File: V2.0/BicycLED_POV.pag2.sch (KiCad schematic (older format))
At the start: 136 parts, among them U10 74x595, U11 74x595, U12 74x595, U13 74x595, U14 74x595, U7 74x595, U8 74x595, U9 74x595

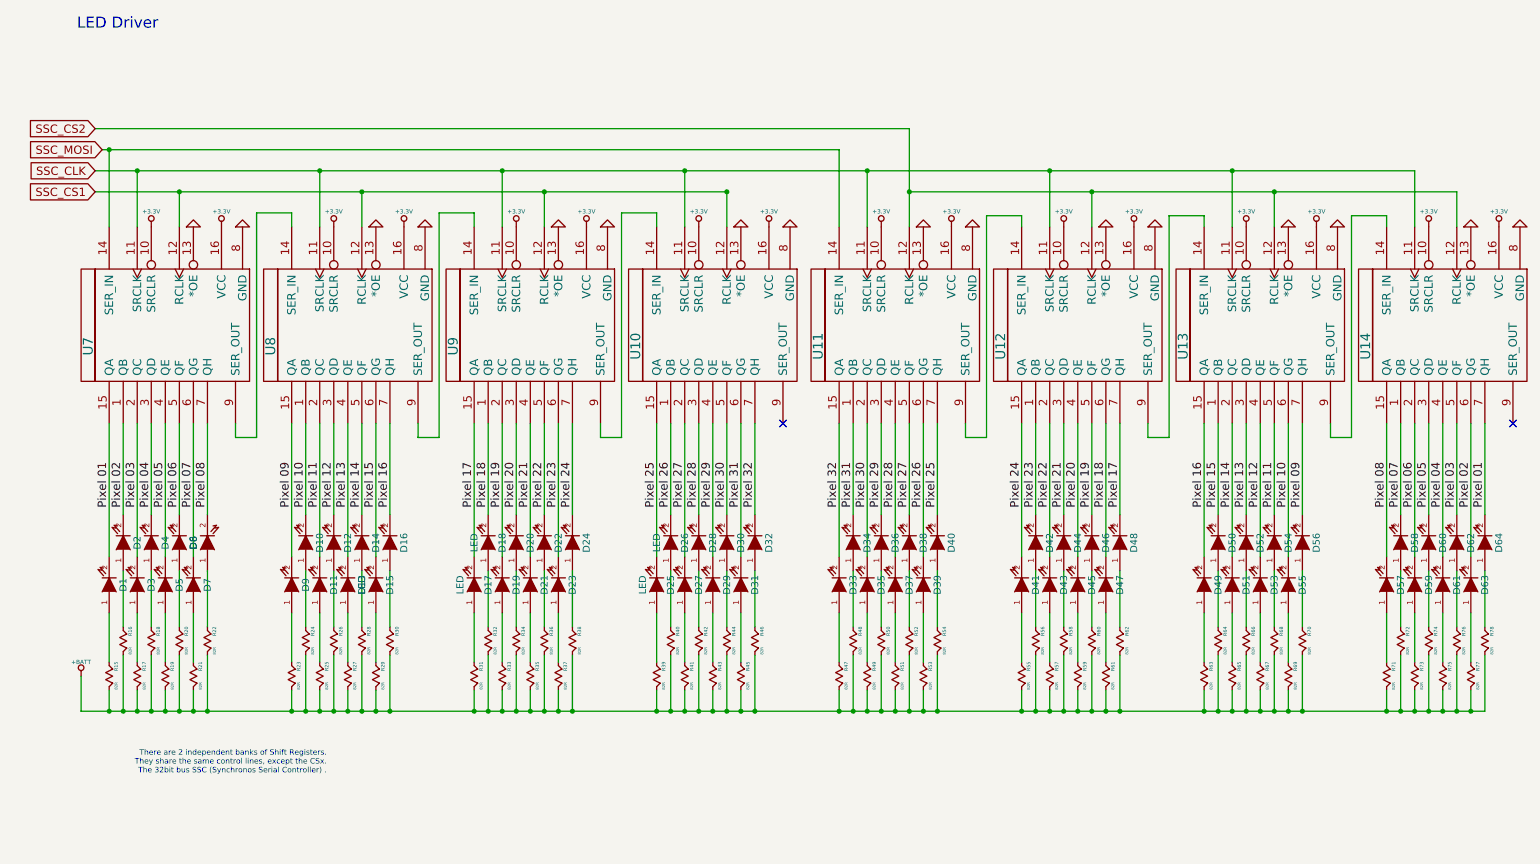
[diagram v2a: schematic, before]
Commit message: Symbols and Modules modifications.
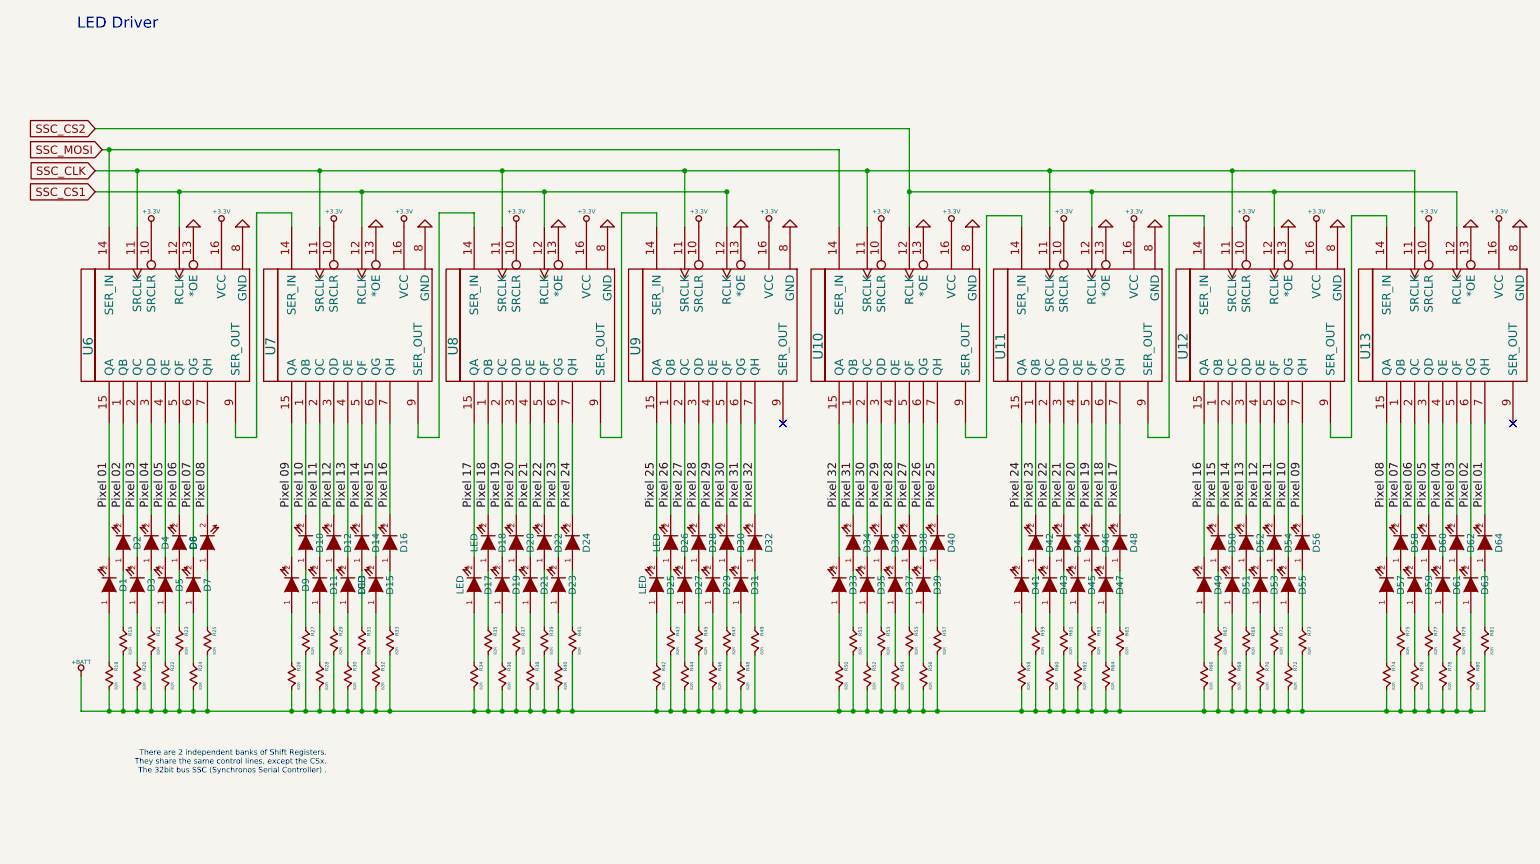
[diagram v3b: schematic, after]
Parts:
- renumbered R15 to R18, R16 to R19, R17 to R20, R18 to R21, R19 to R22, R20 to R23, R21 to R24, R22 to R25, R23 to R26, R24 to R27, R25 to R28, R26 to R29, R27 to R30, R28 to R31, R29 to R32, R30 to R33, R31 to R34, R32 to R35, R33 to R36, R34 to R37, R35 to R38, R36 to R39, R37 to R40, R38 to R41, R39 to R42, R40 to R43, R41 to R44, R42 to R45, R43 to R46, R44 to R47, R45 to R48, R46 to R49, R47 to R50, R48 to R51, R49 to R52, R50 to R53, R51 to R54, R52 to R55, R53 to R56, R54 to R57, R55 to R58, R56 to R59, R57 to R60, R58 to R61, R59 to R62, R60 to R63, R61 to R64, R62 to R65, R63 to R66, R64 to R67, R65 to R68, R66 to R69, R67 to R70, R68 to R71, R69 to R72, R70 to R73, R71 to R74, R72 to R75, R73 to R76, R74 to R77, R75 to R78, R76 to R79, R77 to R80, R78 to R81, U11 to U10, U12 to U11, U13 to U12, U14 to U13, U7 to U6, U8 to U7, U9 to U8, U10 to U9

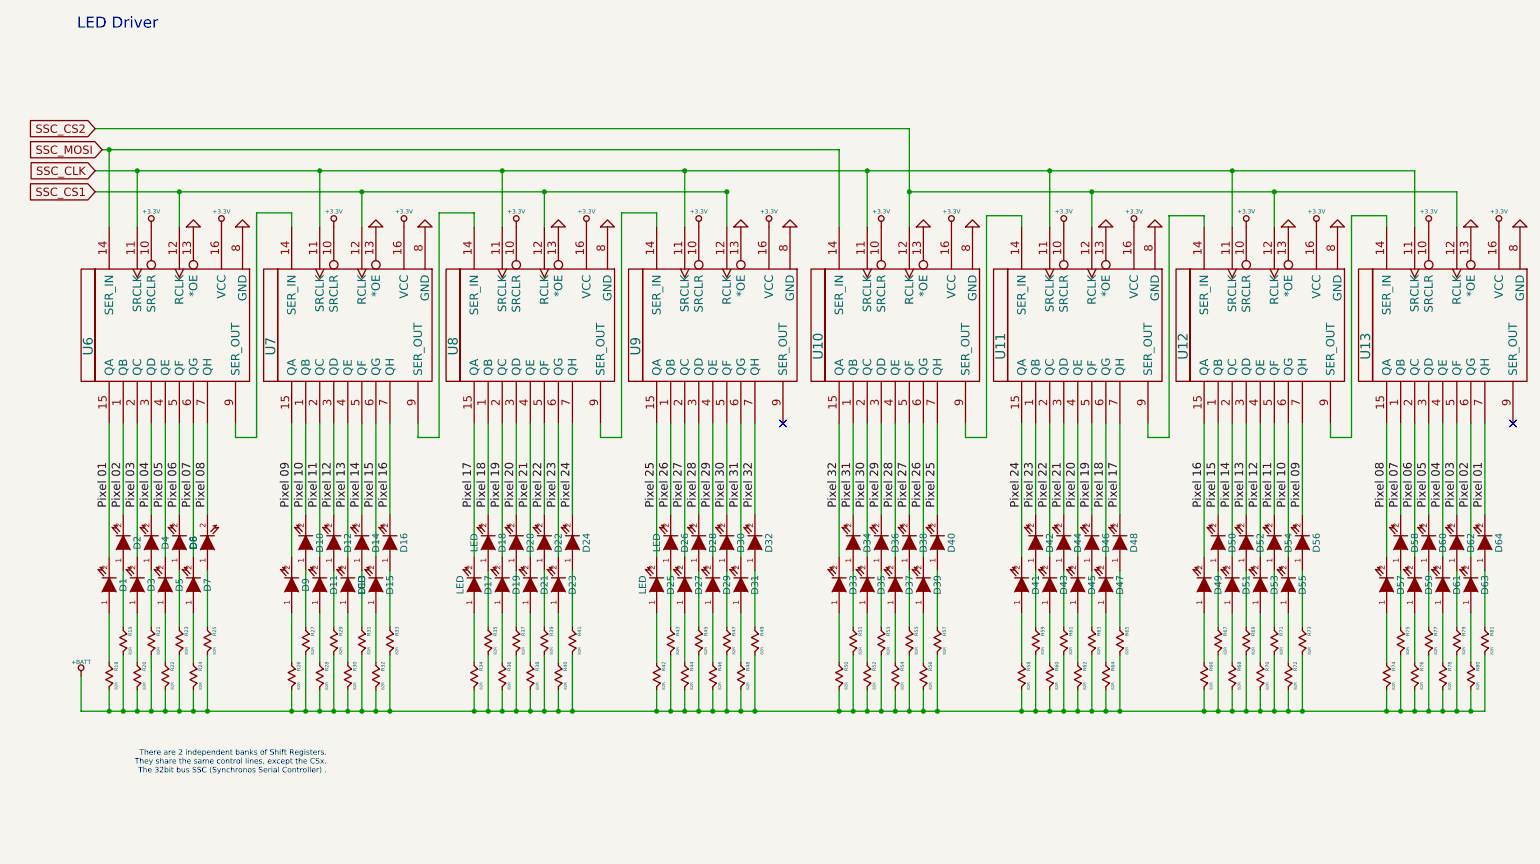
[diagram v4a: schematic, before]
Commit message: 
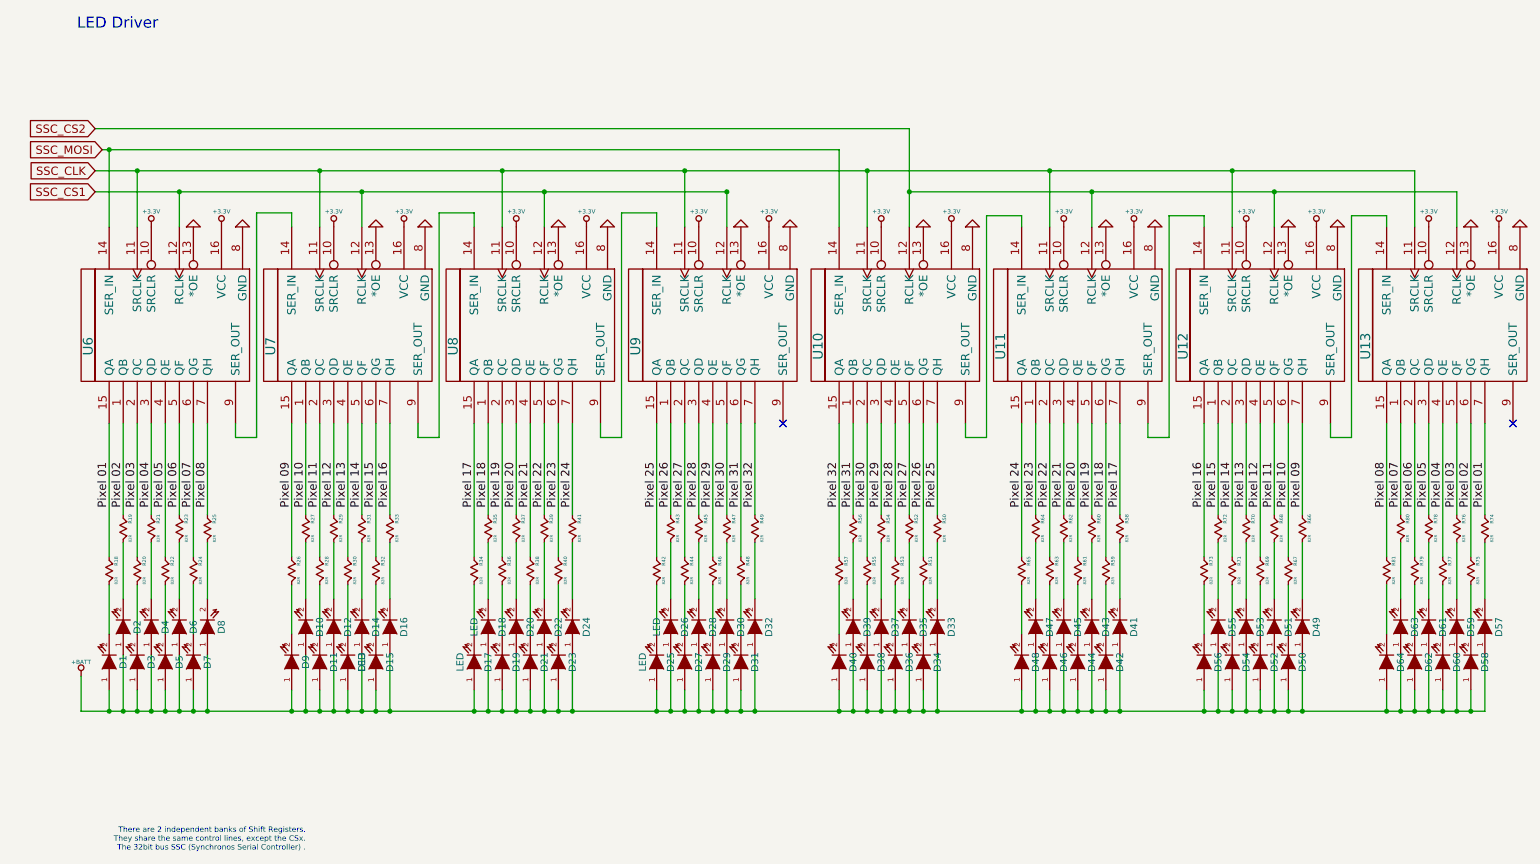
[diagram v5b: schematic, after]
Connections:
- net +BATT: now also D1.1 (A), D10.1 (A), D11.1 (A), D12.1 (A), D13.1 (A), D14.1 (A), D15.1 (A), D16.1 (A), D17.1 (A), D18.1 (A), D19.1 (A), D2.1 (A), D20.1 (A), D21.1 (A), D22.1 (A), D23.1 (A), D24.1 (A), D25.1 (A), D26.1 (A), D27.1 (A), D28.1 (A), D29.1 (A), D3.1 (A), D30.1 (A), D31.1 (A), D32.1 (A), D33.1 (A), D34.1 (A), D35.1 (A), D36.1 (A), D37.1 (A), D38.1 (A), D39.1 (A), D4.1 (A), D40.1 (A), D41.1 (A), D42.1 (A), D43.1 (A), D44.1 (A), D45.1 (A), D46.1 (A), D47.1 (A), D48.1 (A), D49.1 (A), D5.1 (A), D50.1 (A), D51.1 (A), D52.1 (A), D53.1 (A), D54.1 (A), D55.1 (A), D56.1 (A), D57.1 (A), D58.1 (A), D59.1 (A), D6.1 (A), D60.1 (A), D61.1 (A), D62.1 (A), D63.1 (A), D64.1 (A), D7.1 (A), D8.1 (A), D9.1 (A); no longer R18.1 (A), R19.1 (A), R20.1 (A), R21.1 (A), R22.1 (A), R23.1 (A), R24.1 (A), R25.1 (A), R26.1 (A), R27.1 (A), R28.1 (A), R29.1 (A), R30.1 (A), R31.1 (A), R32.1 (A), R33.1 (A), R34.1 (A), R35.1 (A), R36.1 (A), R37.1 (A), R38.1 (A), R39.1 (A), R40.1 (A), R41.1 (A), R42.1 (A), R43.1 (A), R44.1 (A), R45.1 (A), R46.1 (A), R47.1 (A), R48.1 (A), R49.1 (A), R50.1 (A), R51.1 (A), R52.1 (A), R53.1 (A), R54.1 (A), R55.1 (A), R56.1 (A), R57.1 (A), R58.1 (A), R59.1 (A), R60.1 (A), R61.1 (A), R62.1 (A), R63.1 (A), R64.1 (A), R65.1 (A), R66.1 (A), R67.1 (A), R68.1 (A), R69.1 (A), R70.1 (A), R71.1 (A), R72.1 (A), R73.1 (A), R74.1 (A), R75.1 (A), R76.1 (A), R77.1 (A), R78.1 (A), R79.1 (A), R80.1 (A), R81.1 (A)
- net Pixel 01: now also R18.2 (B), R74.2 (B); no longer D1.2 (K), D64.2 (K)
- net Pixel 02: now also R19.2 (B), R75.2 (B); no longer D2.2 (K), D63.2 (K)
- net Pixel 03: now also R20.2 (B), R76.2 (B); no longer D3.2 (K), D62.2 (K)
- net Pixel 04: now also R21.2 (B), R77.2 (B); no longer D4.2 (K), D61.2 (K)
- net Pixel 05: now also R22.2 (B), R78.2 (B); no longer D5.2 (K), D60.2 (K)
- net Pixel 06: now also R23.2 (B), R79.2 (B); no longer D59.2 (K), D6.2 (K)
- net Pixel 07: now also R24.2 (B), R80.2 (B); no longer D58.2 (K), D7.2 (K)
- net Pixel 08: now also R25.2 (B), R81.2 (B); no longer D57.2 (K), D8.2 (K)
- net Pixel 09: now also R26.2 (B), R66.2 (B); no longer D56.2 (K), D9.2 (K)
- net Pixel 10: now also R27.2 (B), R67.2 (B); no longer D10.2 (K), D55.2 (K)
- net Pixel 11: now also R28.2 (B), R68.2 (B); no longer D11.2 (K), D54.2 (K)
- net Pixel 12: now also R29.2 (B), R69.2 (B); no longer D12.2 (K), D53.2 (K)
- net Pixel 13: now also R30.2 (B), R70.2 (B); no longer D13.2 (K), D52.2 (K)
- net Pixel 14: now also R31.2 (B), R71.2 (B); no longer D14.2 (K), D51.2 (K)
- net Pixel 15: now also R32.2 (B), R72.2 (B); no longer D15.2 (K), D50.2 (K)
- net Pixel 16: now also R33.2 (B), R73.2 (B); no longer D16.2 (K), D49.2 (K)
- net Pixel 17: now also R34.2 (B), R58.2 (B); no longer D17.2 (K), D48.2 (K)
- net Pixel 18: now also R35.2 (B), R59.2 (B); no longer D18.2 (K), D47.2 (K)
- net Pixel 19: now also R36.2 (B), R60.2 (B); no longer D19.2 (K), D46.2 (K)
- net Pixel 20: now also R37.2 (B), R61.2 (B); no longer D20.2 (K), D45.2 (K)
- net Pixel 21: now also R38.2 (B), R62.2 (B); no longer D21.2 (K), D44.2 (K)
- net Pixel 22: now also R39.2 (B), R63.2 (B); no longer D22.2 (K), D43.2 (K)
- net Pixel 23: now also R40.2 (B), R64.2 (B); no longer D23.2 (K), D42.2 (K)
- net Pixel 24: now also R41.2 (B), R65.2 (B); no longer D24.2 (K), D41.2 (K)
- net Pixel 25: now also R42.2 (B), R50.2 (B); no longer D25.2 (K), D40.2 (K)
- net Pixel 26: now also R43.2 (B), R51.2 (B); no longer D26.2 (K), D39.2 (K)
- net Pixel 27: now also R44.2 (B), R52.2 (B); no longer D27.2 (K), D38.2 (K)
- net Pixel 28: now also R45.2 (B), R53.2 (B); no longer D28.2 (K), D37.2 (K)
- net Pixel 29: now also R46.2 (B), R54.2 (B); no longer D29.2 (K), D36.2 (K)
- net Pixel 30: now also R47.2 (B), R55.2 (B); no longer D30.2 (K), D35.2 (K)
- net Pixel 31: now also R48.2 (B), R56.2 (B); no longer D31.2 (K), D34.2 (K)
- net Pixel 32: now also R49.2 (B), R57.2 (B); no longer D32.2 (K), D33.2 (K)
- new net: D42.2 (K), R59.1 (A)
- new net: D44.2 (K), R61.1 (A)
- new net: D46.2 (K), R63.1 (A)
- new net: D48.2 (K), R65.1 (A)
- new net: D1.2 (K), R18.1 (A)
- new net: D2.2 (K), R19.1 (A)
- new net: D3.2 (K), R20.1 (A)
- new net: D4.2 (K), R21.1 (A)
- new net: D5.2 (K), R22.1 (A)
- new net: D6.2 (K), R23.1 (A)
- new net: D7.2 (K), R24.1 (A)
- new net: D8.2 (K), R25.1 (A)
- new net: D9.2 (K), R26.1 (A)
- new net: D10.2 (K), R27.1 (A)
- new net: D11.2 (K), R28.1 (A)
- new net: D12.2 (K), R29.1 (A)
- new net: D13.2 (K), R30.1 (A)
- new net: D14.2 (K), R31.1 (A)
- new net: D15.2 (K), R32.1 (A)
- new net: D16.2 (K), R33.1 (A)
- new net: D17.2 (K), R34.1 (A)
- new net: D18.2 (K), R35.1 (A)
- new net: D19.2 (K), R36.1 (A)
- new net: D20.2 (K), R37.1 (A)
- new net: D21.2 (K), R38.1 (A)
- new net: D22.2 (K), R39.1 (A)
- new net: D23.2 (K), R40.1 (A)
- new net: D24.2 (K), R41.1 (A)
- new net: D25.2 (K), R42.1 (A)
- new net: D26.2 (K), R43.1 (A)
- new net: D27.2 (K), R44.1 (A)
- new net: D28.2 (K), R45.1 (A)
- new net: D29.2 (K), R46.1 (A)
- new net: D30.2 (K), R47.1 (A)
- new net: D31.2 (K), R48.1 (A)
- new net: D32.2 (K), R49.1 (A)
- new net: D33.2 (K), R50.1 (A)
- new net: D34.2 (K), R51.1 (A)
- new net: D35.2 (K), R52.1 (A)
- new net: D36.2 (K), R53.1 (A)
- new net: D37.2 (K), R54.1 (A)
- new net: D38.2 (K), R55.1 (A)
- new net: D39.2 (K), R56.1 (A)
- new net: D40.2 (K), R57.1 (A)
- new net: D41.2 (K), R58.1 (A)
- new net: D43.2 (K), R60.1 (A)
- new net: D45.2 (K), R62.1 (A)
- new net: D47.2 (K), R64.1 (A)
- new net: D49.2 (K), R66.1 (A)
- new net: D50.2 (K), R67.1 (A)
- new net: D51.2 (K), R68.1 (A)
- new net: D52.2 (K), R69.1 (A)
- new net: D53.2 (K), R70.1 (A)
- new net: D54.2 (K), R71.1 (A)
- new net: D55.2 (K), R72.1 (A)
- new net: D56.2 (K), R73.1 (A)
- new net: D57.2 (K), R74.1 (A)
- new net: D58.2 (K), R75.1 (A)
- new net: D59.2 (K), R76.1 (A)
- new net: D60.2 (K), R77.1 (A)
- new net: D61.2 (K), R78.1 (A)
- new net: D62.2 (K), R79.1 (A)
- new net: D63.2 (K), R80.1 (A)
- new net: D64.2 (K), R81.1 (A)
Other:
- moved on the sheet: D1, D10, D11, D12, D13, D14, D15, D16, D17, D18, D19, D2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
